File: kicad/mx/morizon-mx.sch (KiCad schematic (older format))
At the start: 116 parts, among them SW1 SW_Push, SW10 SW_Push, SW11 SW_Push, SW12 SW_Push, SW13 SW_Push, SW14 SW_Push, SW15 SW_Push, SW16 SW_Push, SW17 SW_Push, SW18 SW_Push, SW19 SW_Push, SW2 SW_Push, SW20 SW_Push, SW21 SW_Push, SW22 SW_Push, SW23 SW_Push, SW24 SW_Push, SW25 SW_Push, SW26 SW_Push, SW27 SW_Push, SW28 SW_Push, SW29 SW_Push, SW3 SW_Push, SW30 SW_Push, SW31 SW_Push, SW32 SW_Push, SW33 SW_Push, SW34 SW_Push, SW35 SW_Push, SW36 SW_Push, SW37 SW_Push, SW38 SW_Push, SW39 SW_Push, SW4 SW_Push, SW40 SW_Push, SW41 SW_Push, SW42 SW_Push, SW43 SW_Push, SW44 SW_Push, SW45 SW_Push, SW46 SW_Push, SW47 SW_Push, SW48 SW_Push, SW49 SW_Push, SW5 SW_Push, SW50 SW_Push, SW51 SW_Push, SW52 SW_Push, SW6 SW_Push, SW7 SW_Push, SW8 SW_Push, SW9 SW_Push, U1 PRO-MICRO

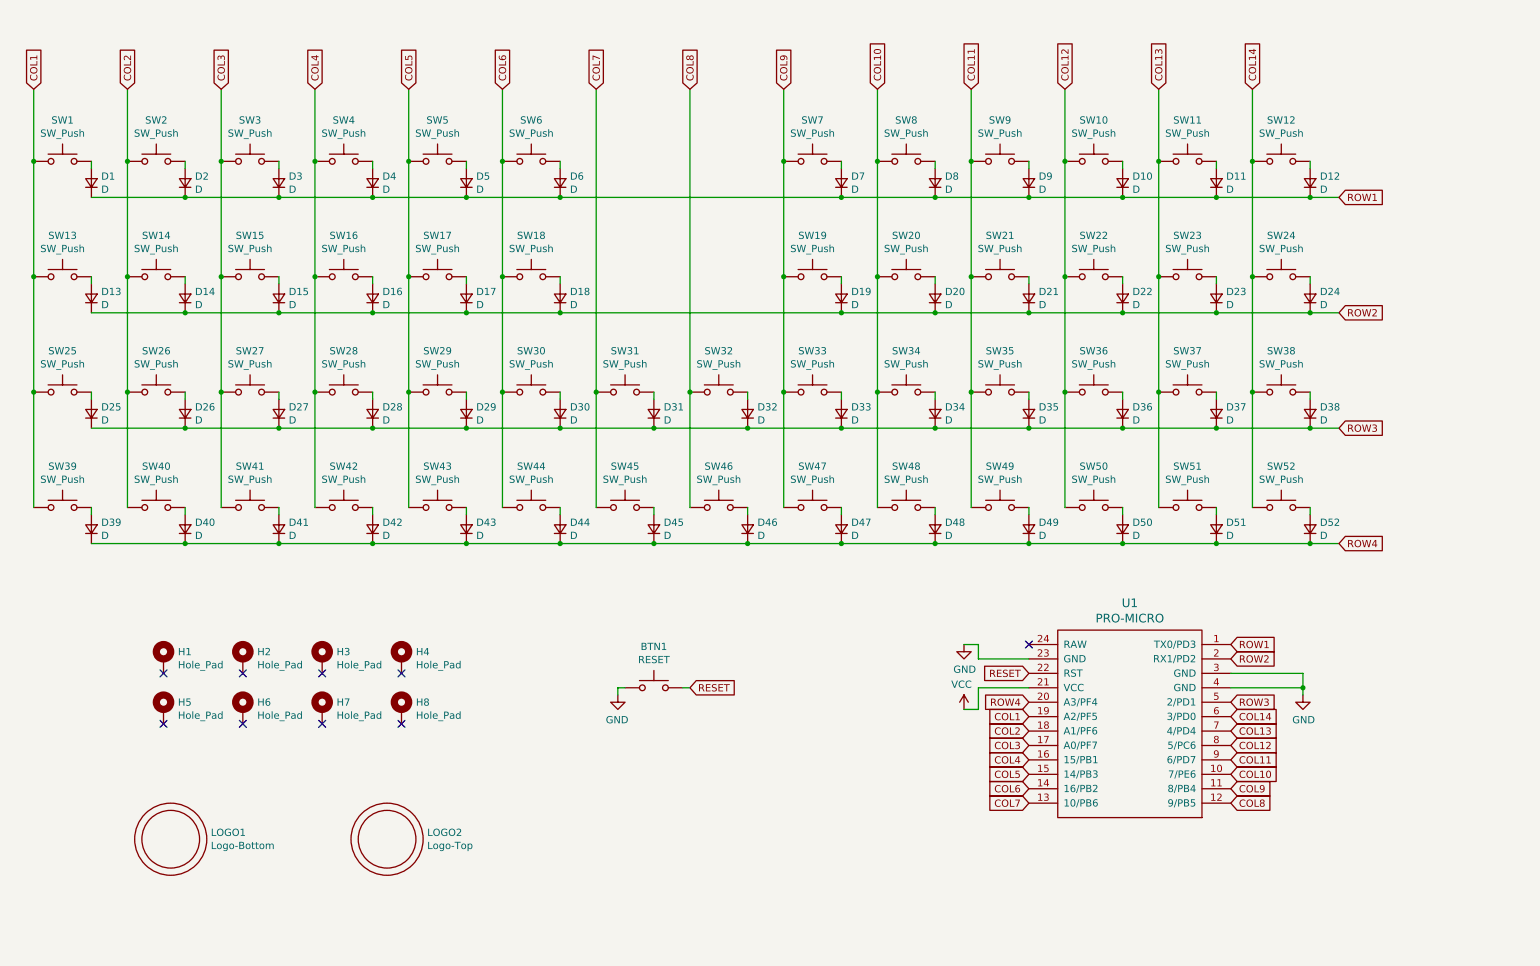
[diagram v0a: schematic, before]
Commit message: Implement Morizon MX
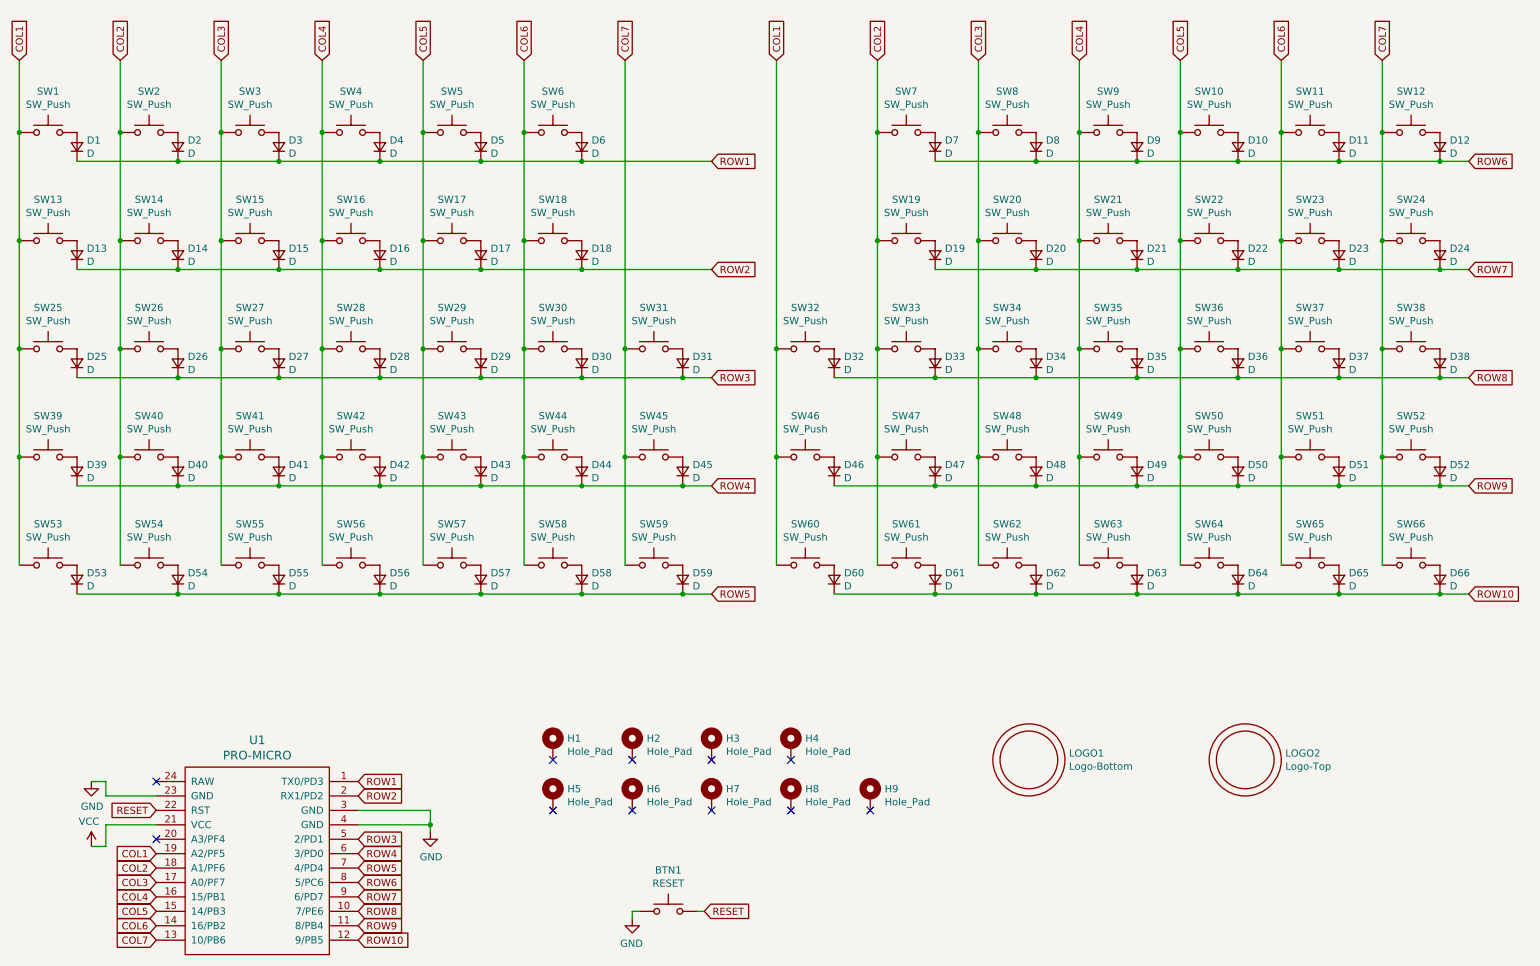
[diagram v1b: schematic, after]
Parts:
- added D53, D54, D55, D56, D57, D58, D59, D60, D61, D62, D63, D64, D65, D66: D, horizon-footprints:D_SOD-123, symbol horizon-components:D
- added H9: Hole_Pad, horizon-footprints:Mount_M2, symbol horizon-components:Hole_Pad
- added SW53, SW54, SW55, SW56, SW57, SW58, SW59, SW60, SW61, SW62, SW63, SW64, SW65, SW66: SW_Push, horizon-footprints:SW_MX, symbol horizon-components:SW_Push
- LOGO1: footprint horizon-footprints:Logo_Horizon_Small -> horizon-footprints:Logo_Morizon_Small
- LOGO2: footprint horizon-footprints:Logo_Horizon_H -> horizon-footprints:Logo_Morizon_M
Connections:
- net COL1: now also SW32.1, SW46.1, SW53.1, SW60.1
- net COL2: now also SW19.1, SW33.1, SW47.1, SW7.1, SW54.1, SW61.1
- net COL3: now also SW20.1, SW34.1, SW48.1, SW8.1, SW55.1, SW62.1
- net COL4: now also SW21.1, SW35.1, SW49.1, SW9.1, SW56.1, SW63.1
- net COL5: now also SW10.1, SW22.1, SW36.1, SW50.1, SW57.1, SW64.1
- net COL6: now also SW11.1, SW23.1, SW37.1, SW51.1, SW58.1, SW65.1
- net COL7: now also SW12.1, SW24.1, SW38.1, SW52.1, SW59.1, SW66.1
- net ROW1: no longer D10.1 (K), D11.1 (K), D12.1 (K), D7.1 (K), D8.1 (K), D9.1 (K)
- net ROW2: no longer D19.1 (K), D20.1 (K), D21.1 (K), D22.1 (K), D23.1 (K), D24.1 (K)
- net ROW3: no longer D32.1 (K), D33.1 (K), D34.1 (K), D35.1 (K), D36.1 (K), D37.1 (K), D38.1 (K)
- net ROW4: now also U1.6 (3/PD0); no longer D46.1 (K), D47.1 (K), D48.1 (K), D49.1 (K), D50.1 (K), D51.1 (K), D52.1 (K), U1.20 (A3/PF4)
- removed net COL10: SW20.1, SW34.1, SW48.1, SW8.1, U1.10 (7/PE6)
- removed net COL11: SW21.1, SW35.1, SW49.1, SW9.1, U1.9 (6/PD7)
- removed net COL12: SW10.1, SW22.1, SW36.1, SW50.1, U1.8 (5/PC6)
- removed net COL13: SW11.1, SW23.1, SW37.1, SW51.1, U1.7 (4/PD4)
- removed net COL14: SW12.1, SW24.1, SW38.1, SW52.1, U1.6 (3/PD0)
- removed net COL8: SW32.1, SW46.1, U1.12 (9/PB5)
- removed net COL9: SW19.1, SW33.1, SW47.1, SW7.1, U1.11 (8/PB4)
- new net: D53.2 (A), SW53.2
- new net: D54.2 (A), SW54.2
- new net: D55.2 (A), SW55.2
- new net: D56.2 (A), SW56.2
- new net: D57.2 (A), SW57.2
- new net: D58.2 (A), SW58.2
- new net: D59.2 (A), SW59.2
- new net: D60.2 (A), SW60.2
- new net: D61.2 (A), SW61.2
- new net: D62.2 (A), SW62.2
- new net: D63.2 (A), SW63.2
- new net: D64.2 (A), SW64.2
- new net: D65.2 (A), SW65.2
- new net: D66.2 (A), SW66.2
- new net ROW10: D60.1 (K), D61.1 (K), D62.1 (K), D63.1 (K), D64.1 (K), D65.1 (K), D66.1 (K), U1.12 (9/PB5)
- new net ROW5: D53.1 (K), D54.1 (K), D55.1 (K), D56.1 (K), D57.1 (K), D58.1 (K), D59.1 (K), U1.7 (4/PD4)
- new net ROW6: D10.1 (K), D11.1 (K), D12.1 (K), D7.1 (K), D8.1 (K), D9.1 (K), U1.8 (5/PC6)
- new net ROW7: D19.1 (K), D20.1 (K), D21.1 (K), D22.1 (K), D23.1 (K), D24.1 (K), U1.9 (6/PD7)
- new net ROW8: D32.1 (K), D33.1 (K), D34.1 (K), D35.1 (K), D36.1 (K), D37.1 (K), D38.1 (K), U1.10 (7/PE6)
- new net ROW9: D46.1 (K), D47.1 (K), D48.1 (K), D49.1 (K), D50.1 (K), D51.1 (K), D52.1 (K), U1.11 (8/PB4)
- no-connect marks 9 -> 11
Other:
- moved on the sheet: BTN1, D1, D2, H1, H2, H3, H4, H5, H6, H7, H8, LOGO1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
